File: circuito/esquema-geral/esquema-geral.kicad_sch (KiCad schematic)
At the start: 18 parts, among them J1 Alimentação, J2 COMPUTADOR, J3 POTÊNCIA, J4 COMPUTADOR, J5 POTÊNCIA, SW1 SELETOR, SW2 CIRCUITO COMPUTADOR, SW3 CIRCUITO POTÊNCIA, SW4 BATERIA, SW5 CIRCUITO COMPUTADOR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

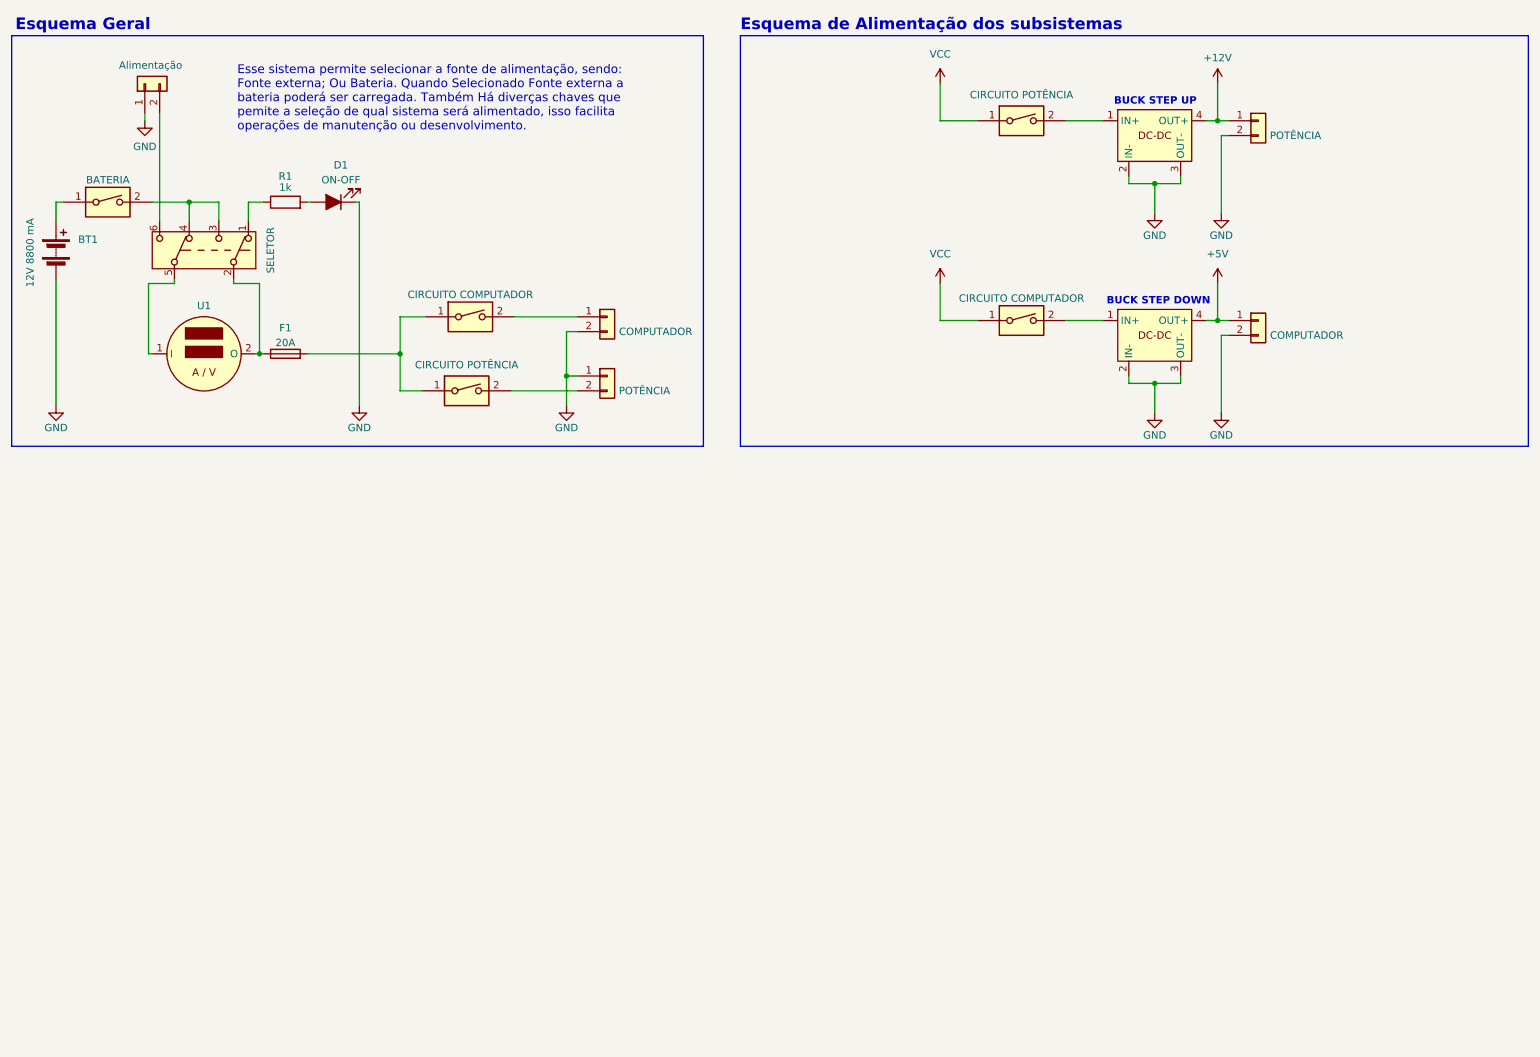
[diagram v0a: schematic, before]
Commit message: dog dos esquemas de alimentação e conexões gerais
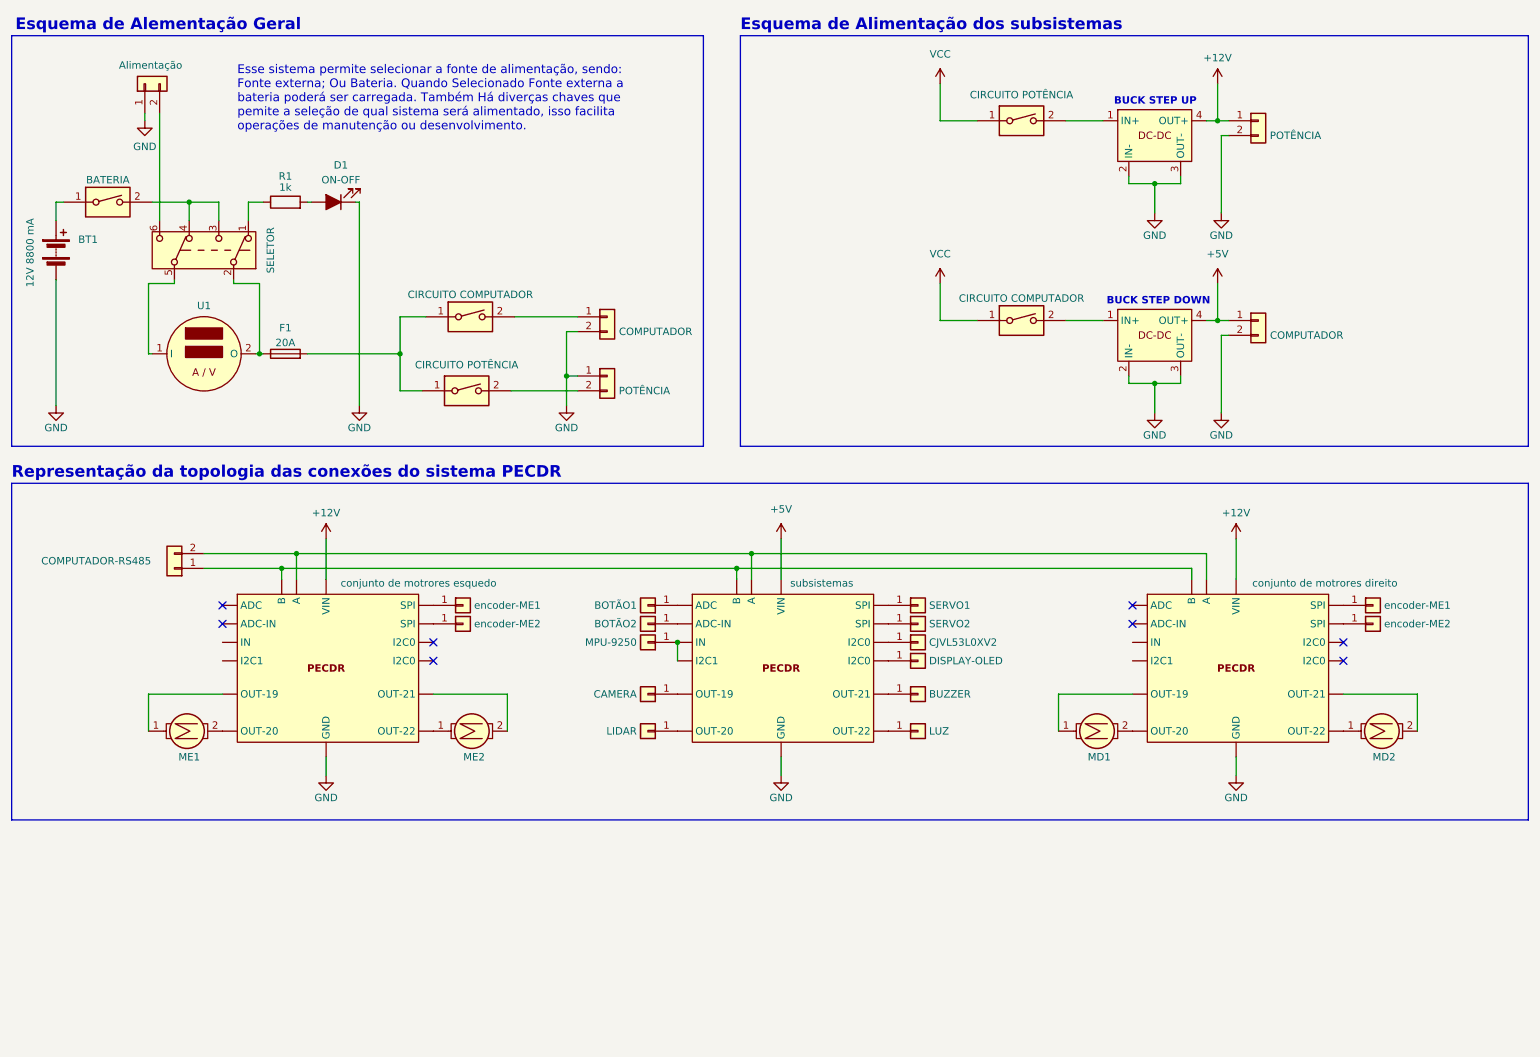
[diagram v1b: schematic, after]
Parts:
- added J10, J6: encoder-ME1, symbol Connector_Generic:Conn_01x01
- added J11, J7: encoder-ME2, symbol Connector_Generic:Conn_01x01
- added J12: LIDAR, symbol Connector_Generic:Conn_01x01
- added J13: BUZZER, symbol Connector_Generic:Conn_01x01
- added J14: LUZ, symbol Connector_Generic:Conn_01x01
- added J15: MPU-9250, symbol Connector_Generic:Conn_01x01
- added J16: CJVL53L0XV2, symbol Connector_Generic:Conn_01x01
- added J17: SERVO1, symbol Connector_Generic:Conn_01x01
- added J18: SERVO2, symbol Connector_Generic:Conn_01x01
- added J19: BOTÃO1, symbol Connector_Generic:Conn_01x01
- added J20: BOTÃO2, symbol Connector_Generic:Conn_01x01
- added J21: DISPLAY-OLED, symbol Connector_Generic:Conn_01x01
- added J8: COMPUTADOR-RS485, symbol Connector_Generic:Conn_01x02
- added J9: CAMERA, symbol Connector_Generic:Conn_01x01
- added M1: ME2, symbol Motor:Motor_DC_ALT
- added M2: ME1, symbol Motor:Motor_DC_ALT
- added M5: MD1, symbol Motor:Motor_DC_ALT
- added M6: MD2, symbol Motor:Motor_DC_ALT
- added U4: conjunto de motrores esquedo, symbol MyLib2-ALL:PECDR
- added U5: subsistemas, symbol MyLib2-ALL:PECDR
- added U6: conjunto de motrores direito, symbol MyLib2-ALL:PECDR
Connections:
- net +12V: now also U4. (VIN), U6. (VIN)
- net +5V: now also U5. (VIN)
- net GND: now also U4. (VIN), U5. (VIN), U6. (VIN)
- new net: M5.1, U6. (VIN)
- new net: M5.2, U6. (VIN)
- new net: J13.1 (Pin_1), U5. (VIN)
- new net: J10.1 (Pin_1), U6. (VIN)
- new net: M6.1, U6. (VIN)
- new net: M6.2, U6. (VIN)
- new net: J14.1 (Pin_1), U5. (VIN)
- new net: J8.1 (Pin_1), U4. (VIN), U5. (VIN), U6. (VIN)
- new net: J8.2 (Pin_2), U4. (VIN), U5. (VIN), U6. (VIN)
- new net: J20.1 (Pin_1), U5. (VIN)
- new net: J16.1 (Pin_1), U5. (VIN)
- new net: J18.1 (Pin_1), U5. (VIN)
- new net: J9.1 (Pin_1), U5. (VIN)
- new net: J21.1 (Pin_1), U5. (VIN)
- new net: J12.1 (Pin_1), U5. (VIN)
- new net: J15.1 (Pin_1), U5. (VIN)
- new net: J19.1 (Pin_1), U5. (VIN)
- new net: J17.1 (Pin_1), U5. (VIN)
- new net: J6.1 (Pin_1), U4. (VIN)
- new net: J11.1 (Pin_1), U6. (VIN)
- new net: M1.1, U4. (VIN)
- new net: M1.2, U4. (VIN)
- new net: M2.1, U4. (VIN)
- new net: M2.2, U4. (VIN)
- new net: J7.1 (Pin_1), U4. (VIN)
- no-connect marks 0 -> 8
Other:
- note added: "Esquema de Alementação Geral"
- note added: "Representação da topologia das conexões do sistema PECDR"
- note removed: "Esquema Geral"

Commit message: arrumando doc
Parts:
- J10: value encoder-ME1 -> encoder-MD1
- J11: value encoder-ME2 -> encoder-MD2
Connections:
- new net: J8.1 (Pin_1), U4. (VIN), U5. (VIN), U6. (VIN)
- new net: J8.2 (Pin_2), U4. (VIN), U5. (VIN), U6. (VIN)
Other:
- note added: "Esse sistema permite selecionar a fonte de alimentação, sendo: Fonte externa; Ou Bateria. Quando Selecionado Fonte externa a bateria poderá ser carregada. Também Há diversas chaves que permite a seleção de qual sistema será alimentado, isso facilita operações de manutenção ou desenvolvimento."
- note removed: "Esse sistema permite selecionar a fonte de alimentação, sendo: Fonte externa; Ou Bateria. Quando Selecionado Fonte externa a bateria poderá ser carregada. Também Há diverças chaves que pemite a seleção de qual sistema será alimentado, isso facilita operações de manutenção ou desenvolvimento."
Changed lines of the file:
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@@
     (fill (type none))
   )
-  (text "Esse sistema permite selecionar a fonte de alimentação, sendo:\nFonte externa; Ou Bateria. Quando Selecionado Fonte externa a\nbateria poderá ser carregada. Também Há diverças chaves que\npemite a seleção de qual sistema será alimentado, isso facilita\noperações de manutenção ou desenvolvimento."
+  (text "Esse sistema permite selecionar a fonte de alimentação, sendo:\nFonte externa; Ou Bateria. Quando Selecionado Fonte externa a\nbateria poderá ser carregada. Também Há diversas chaves que\npermite a seleção de qual sistema será alimentado, isso facilita\noperações de manutenção ou desenvolvimento."
     (at 57.15 34.925 0)
     (effects (font (size 1.5 1.5)) (justify left bottom))
@@
       (effects (font (size 1.27 1.27)) (justify left) hide)
     )
-    (property "Value" "encoder-ME1" (at 254 116.205 0)
+    (property "Value" "encoder-MD1" (at 254 116.205 0)
       (effects (font (size 1.27 1.27)) (justify left))
     )
@@
       (effects (font (size 1.27 1.27)) (justify left) hide)
     )
-    (property "Value" "encoder-ME2" (at 254 119.38 0)
+    (property "Value" "encoder-MD2" (at 254 119.38 0)
       (effects (font (size 1.27 1.27)) (justify left))
     )

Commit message: arrumando doc
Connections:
- new net: J8.1 (Pin_1), U4. (VIN), U5. (VIN), U6. (VIN)
- new net: J8.2 (Pin_2), U4. (VIN), U5. (VIN), U6. (VIN)
- no-connect marks 8 -> 12
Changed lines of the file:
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@@
   (no_connect (at 54.61 116.205))
   (no_connect (at 210.82 119.38))
+  (no_connect (at 210.82 122.555))
   (no_connect (at 210.82 116.205))
   (no_connect (at 54.61 119.38))
+  (no_connect (at 54.61 122.555))
   (no_connect (at 90.805 125.73))
+  (no_connect (at 210.82 125.73))
   (no_connect (at 247.015 122.555))
+  (no_connect (at 54.61 125.73))
   (wire (pts (xy 46.355 60.325) (xy 46.355 60.96))
     (stroke (width 0) (type default))

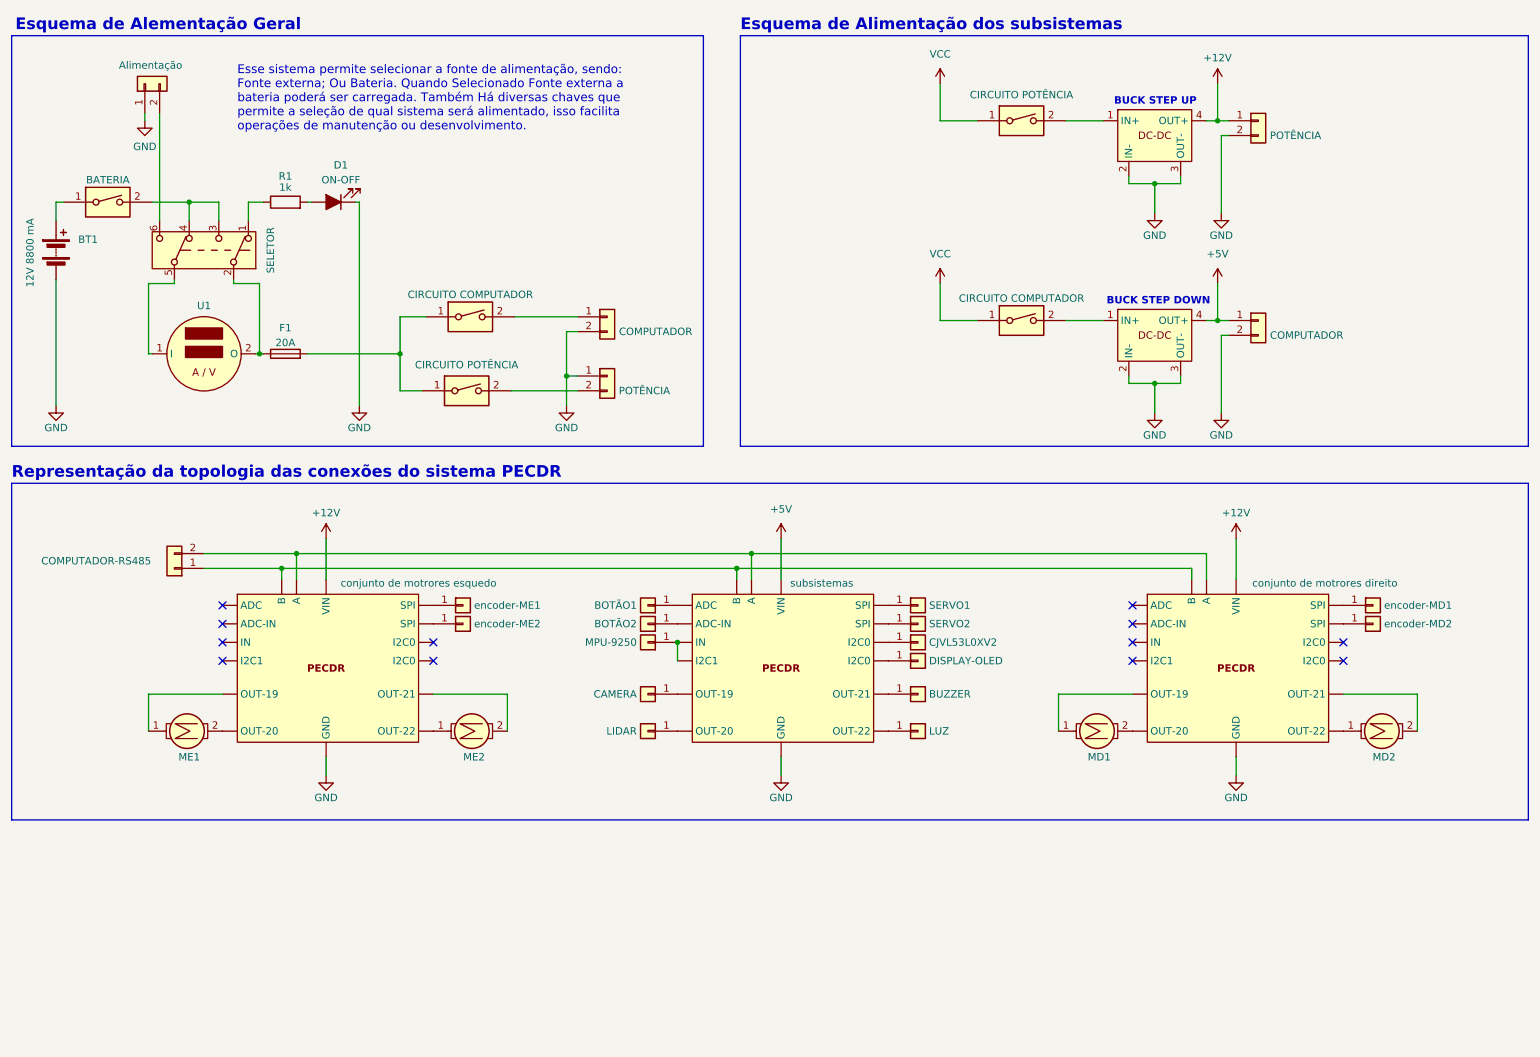
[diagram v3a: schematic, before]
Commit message: PECDR correção rs485 e de layout
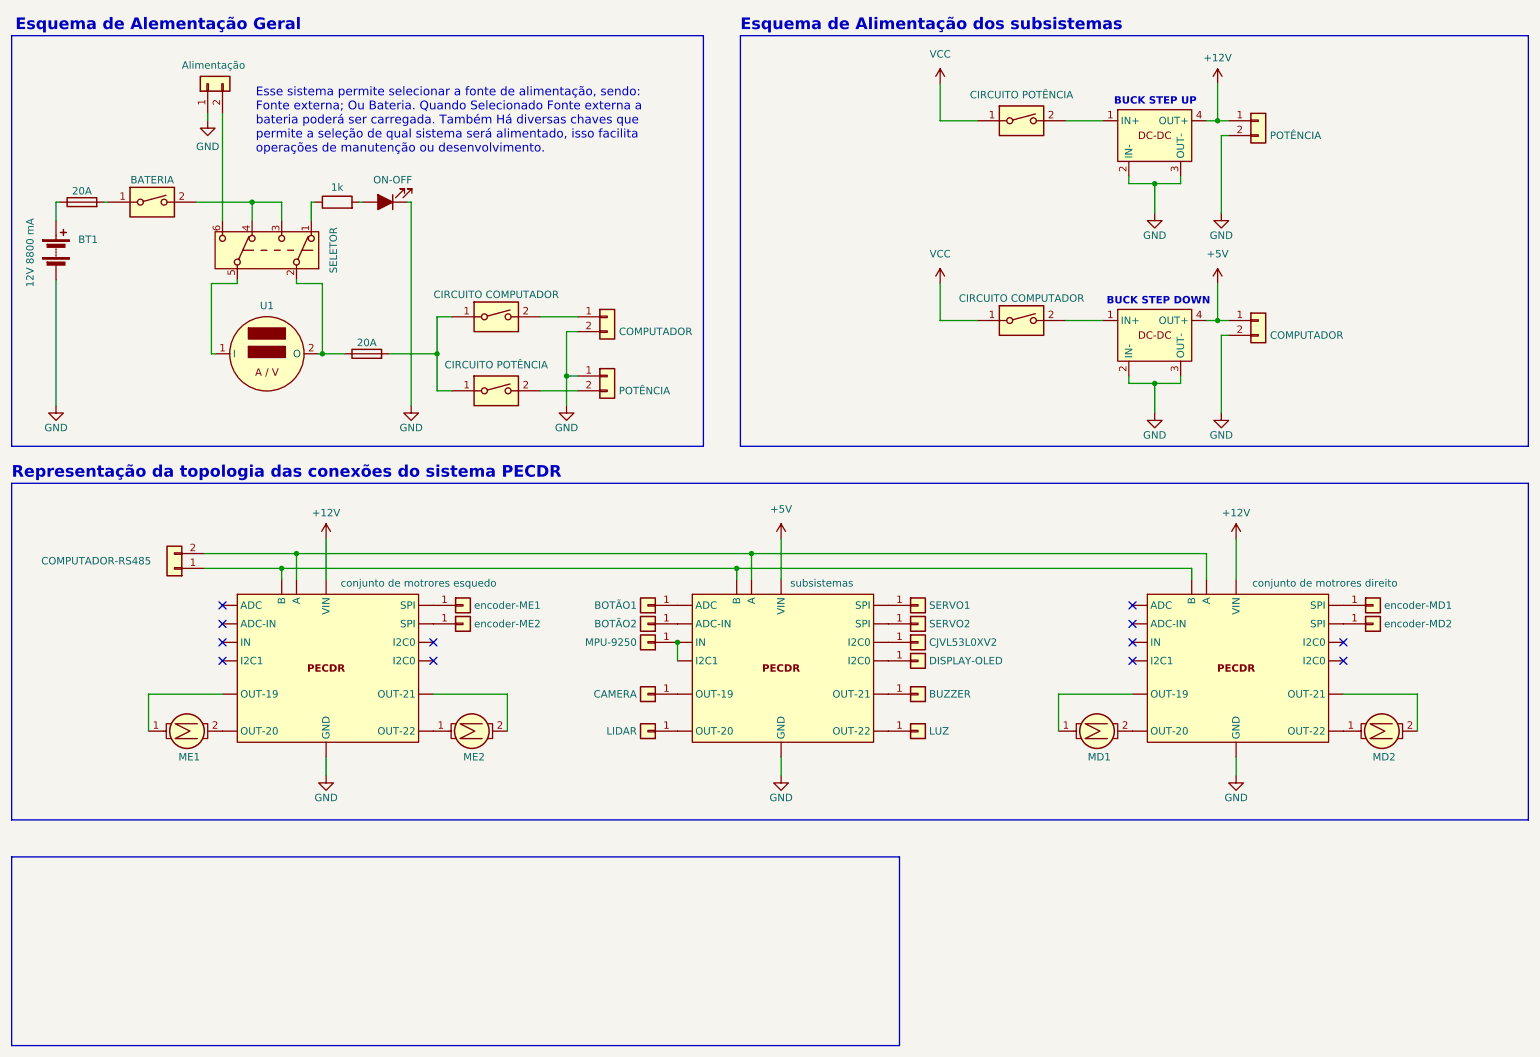
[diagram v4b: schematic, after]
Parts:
- added F2: 20A, symbol Device:Fuse
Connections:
- net at BT1.1 (+): now also F2.1; no longer SW4.1
- new net: F2.2, SW4.1
- new net: J8.1 (Pin_1), U4. (VIN), U5. (VIN), U6. (VIN)
- new net: J8.2 (Pin_2), U4. (VIN), U5. (VIN), U6. (VIN)
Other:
- moved on the sheet: U1

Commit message: atualização do esquema geral
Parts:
- removed D1: ON-OFF, symbol Device:LED_Filled
- removed F1, F2: 20A, symbol Device:Fuse
- removed J2: COMPUTADOR, symbol Connector_Generic:Conn_01x02
- removed J3: POTÊNCIA, symbol Connector_Generic:Conn_01x02
- removed SW4: BATERIA, symbol Switch:SW_DIP_x01
- removed U2: ~, symbol MyLib2-ALL:DC-DC
- added BT1: 12V 8A8, symbol Device:Battery
- added J2: bdesc-ME1, symbol Connector_Generic:Conn_01x01
- added J22: bdesc-MD2, symbol Connector_Generic:Conn_01x01
- added J23: bdesc-MD1, symbol Connector_Generic:Conn_01x01
- added J3: bdesc-ME2, symbol Connector_Generic:Conn_01x01
- added M3, M9: bdesc-MD1, symbol Motor:Motor_DC_ALT
- added M4: bdesc-ME1, symbol Motor:Motor_DC_ALT
- added M8: bdesc-ME2, symbol Motor:Motor_DC_ALT
- added R3: CARGA, symbol Device:R
- BT2: renamed from BT1; value 12V 8800 mA -> 12V 8A8
- J21: value DISPLAY-OLED -> GPRS-GNSS
- R1: value 1k -> CARGA
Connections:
- net +12V: now also SW6.2, M3.3, M4.3, M8.3, M9.3
- net GND: no longer BT2.2 (-), J1.1 (Pin_1)
- net at BT2.1 (+): now also SW1.5 (B), BT1.1 (+)
- net at M5.1: now also M9.1; no longer U6. (VIN)
- net at M5.2: now also M9.2; no longer U6. (VIN)
- net at SW1.1 (A): now also R1.2, U1.1 (I), R3.2; no longer R1.1
- net at SW1.2 (B): now also BT2.2 (-), BT1.2 (-); no longer U1.2 (O)
- net at SW1.3 (C): now also J1.2 (Pin_2), U1.2 (O); no longer SW1.4 (A)
- net at SW1.6 (C): now also J1.1 (Pin_1), SW1.4 (A), SW2.1, SW3.1; no longer J1.2 (Pin_2)
- net at SW3.2: now also R1.1
- net at M6.1: now also M3.1; no longer U6. (VIN)
- net at M6.2: now also M3.2; no longer U6. (VIN)
- net at J14.1 (Pin_1): now also U6. (VIN); no longer U5. (VIN)
- net at J20.1 (Pin_1): now also U6. (VIN); no longer U5. (VIN)
- net USB-JETSON-NANO: now reaches J21.1 (Pin_1)
- net USB-JETSON-NANO: now also J12.1 (Pin_1); no longer U5. (VIN)
- net at J19.1 (Pin_1): now also U4. (VIN); no longer U5. (VIN)
- net at SW2.2: now also R3.1
- net at M1.1: now also M8.1; no longer U4. (VIN)
- net at M1.2: now also M8.2; no longer U4. (VIN)
- net at M2.1: now also M4.1; no longer U4. (VIN)
- net at M2.2: now also M4.2; no longer U4. (VIN)
- new net: J3.1 (Pin_1), U4. (VIN)
- new net: J23.1 (Pin_1), U6. (VIN)
- new net: J2.1 (Pin_1), U4. (VIN)
- new net: J8.1 (Pin_1), U4. (VIN), U5. (VIN), U6. (VIN)
- new net: J8.2 (Pin_2), U4. (VIN), U5. (VIN), U6. (VIN)
- new net: J22.1 (Pin_1), U6. (VIN)
- no-connect marks 12 -> 18
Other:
- note added: "Esse sistema permite selecionar se a bateria irá passr pelo voltimetro-amperimetro, ou se firará em paralelo com a carga, permitindo assim monitorar o carregamento da bateria. Também Há diversas chaves que permite a seleção de qual sistema será alimentado, isso facilita operações de manutenção ou desenvolvimento."
- note added: "Representação da topologia das conexões do motor e dos circuitos de potência"
- note removed: "BUCK STEP UP"
- note removed: "Esse sistema permite selecionar a fonte de alimentação, sendo: Fonte externa; Ou Bateria. Quando Selecionado Fonte externa a bateria poderá ser carregada. Também Há diversas chaves que permite a seleção de qual sistema será alimentado, isso facilita operações de manutenção ou desenvolvimento."
- moved on the sheet: BT2, U1
